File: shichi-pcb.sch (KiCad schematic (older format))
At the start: 27 parts, among them J1 USB_C_Receptacle_HRO_TYPE-C-3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, J2 Conn_01x04_Male, J3 Conn_01x06_Male, J4 Conn_01x04_Male, J5 Conn_01x02_Male, J6 Conn_01x01_Male, SW1 SW_Push, SW2 SW_Push, U1 MCP1700-3302E_SOT23, U2 USBLC6-2SC6, U3 STM32F072CBTx

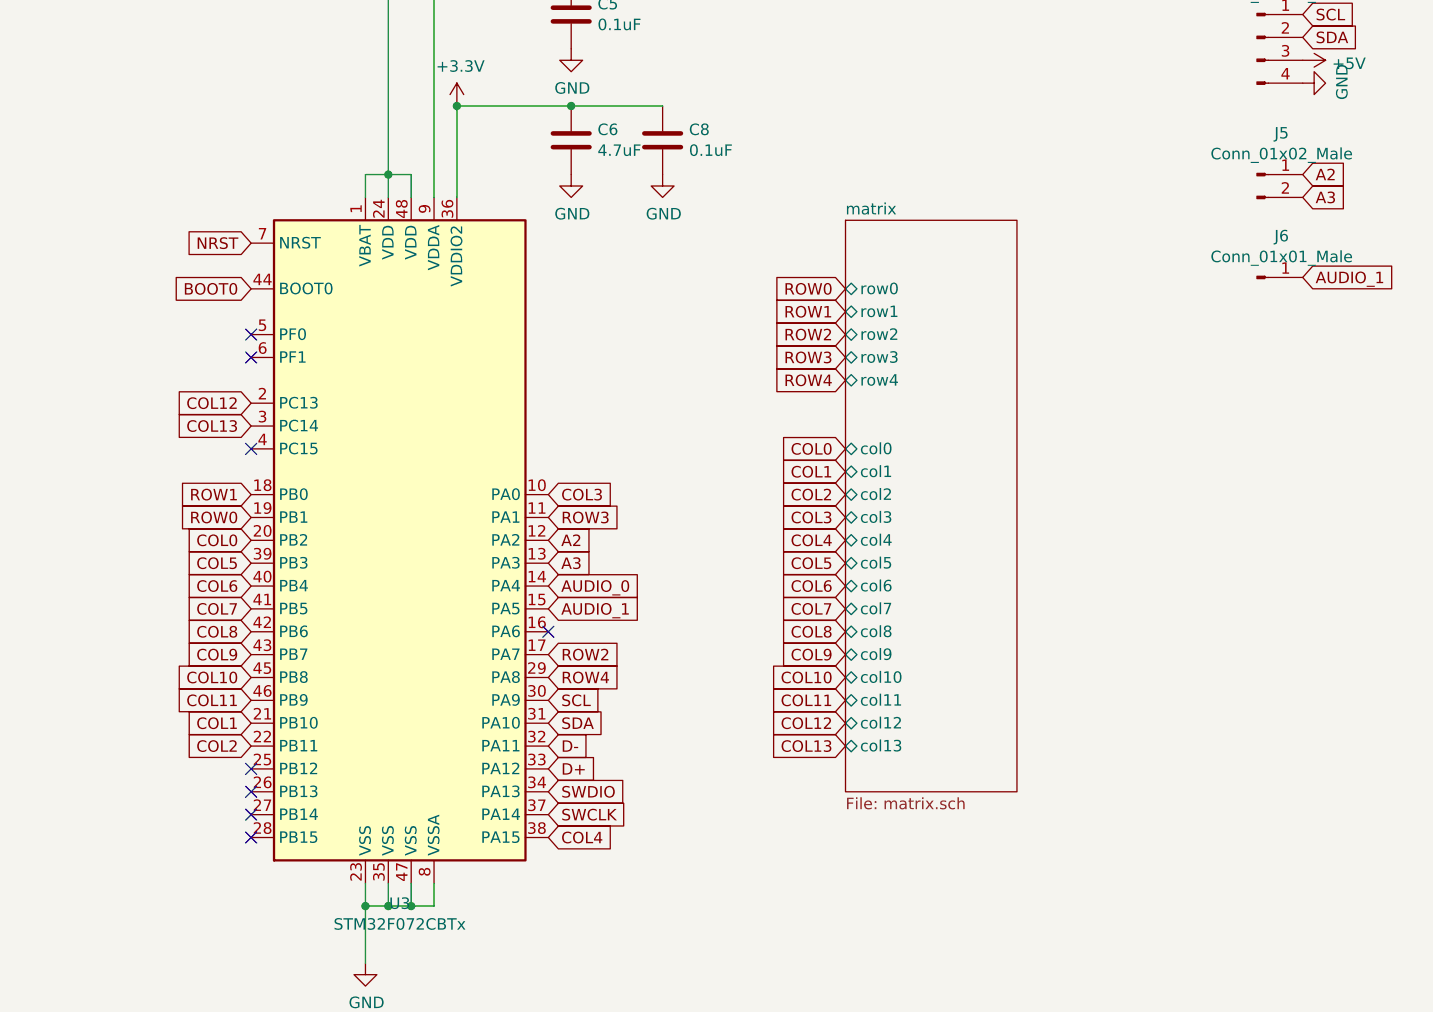
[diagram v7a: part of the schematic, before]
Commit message: Optimize STM32F072 matrix pinout
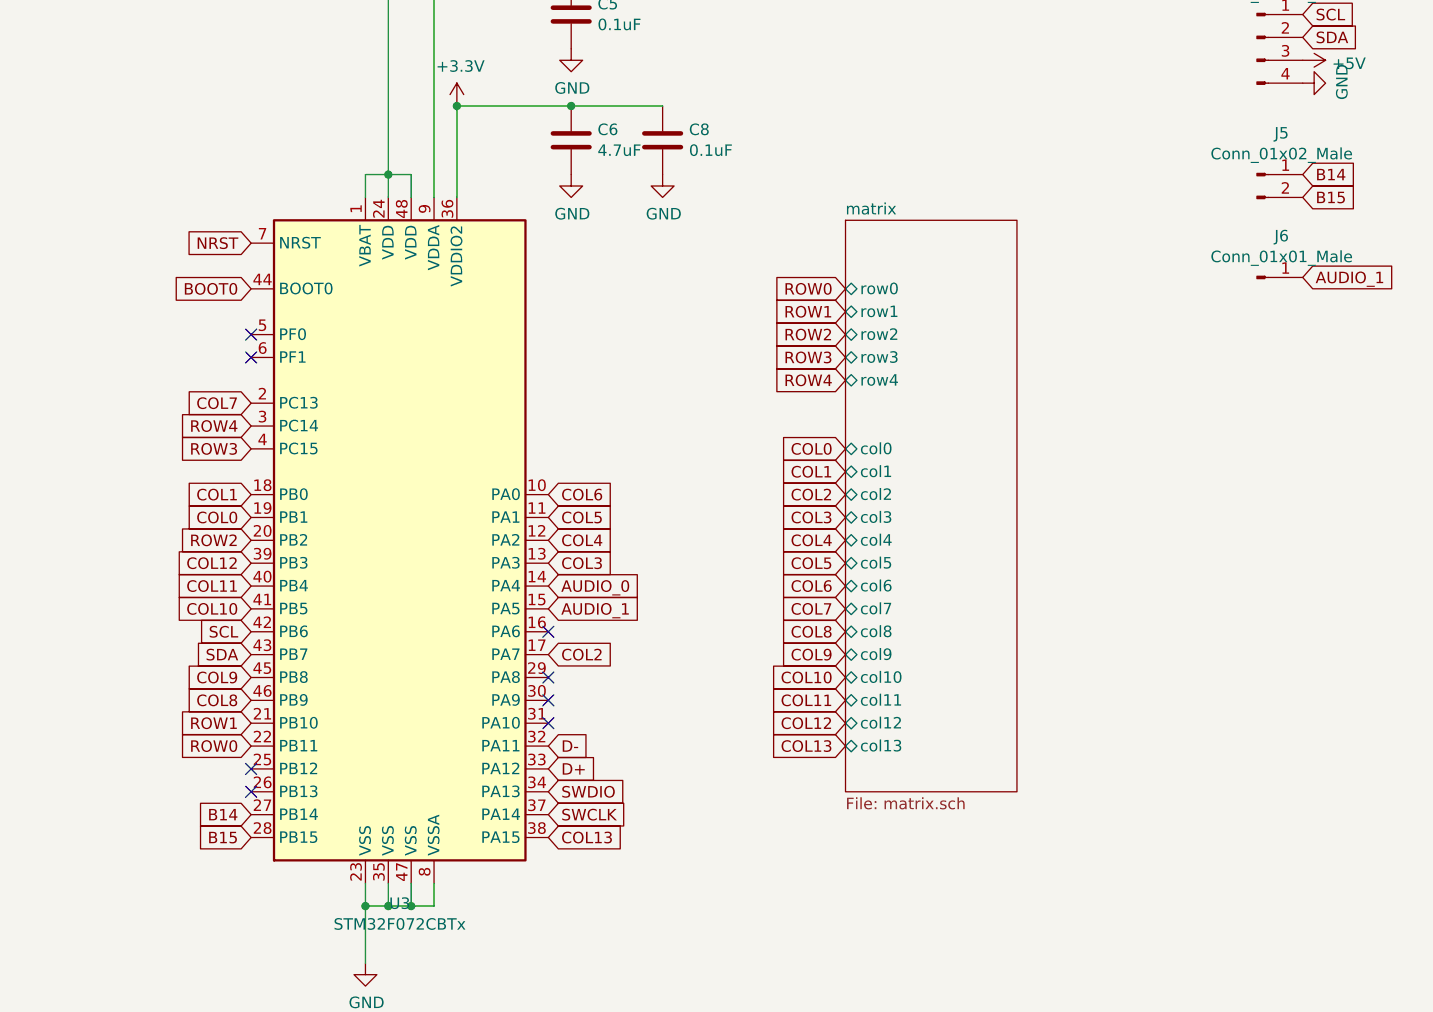
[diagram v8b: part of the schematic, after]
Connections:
- net COL0: now also U3.19 (PB1); no longer U3.20 (PB2)
- net COL1: now also U3.18 (PB0); no longer U3.21 (PB10)
- net COL10: now also U3.41 (PB5); no longer U3.45 (PB8)
- net COL11: now also U3.40 (PB4); no longer U3.46 (PB9)
- net COL12: now also U3.39 (PB3); no longer U3.2 (PC13)
- net COL13: now also U3.38 (PA15); no longer U3.3 (PC14)
- net COL2: now also U3.17 (PA7); no longer U3.22 (PB11)
- net COL3: now also U3.13 (PA3); no longer U3.10 (PA0)
- net COL4: now also U3.12 (PA2); no longer U3.38 (PA15)
- net COL5: now also U3.11 (PA1); no longer U3.39 (PB3)
- net COL6: now also U3.10 (PA0); no longer U3.40 (PB4)
- net COL7: now also U3.2 (PC13); no longer U3.41 (PB5)
- net COL8: now also U3.46 (PB9); no longer U3.42 (PB6)
- net COL9: now also U3.45 (PB8); no longer U3.43 (PB7)
- net ROW0: now also U3.22 (PB11); no longer U3.19 (PB1)
- net ROW1: now also U3.21 (PB10); no longer U3.18 (PB0)
- net ROW2: now also U3.20 (PB2); no longer U3.17 (PA7)
- net ROW3: now also U3.4 (PC15); no longer U3.11 (PA1)
- net ROW4: now also U3.3 (PC14); no longer U3.29 (PA8)
- net SCL: now also U3.42 (PB6); no longer U3.30 (PA9)
- net SDA: now also U3.43 (PB7); no longer U3.31 (PA10)
- net B14: now reaches U3.27 (PB14)
- net B14: now also J5.1 (Pin_1)
- net B15: now reaches U3.28 (PB15)
- net B15: now also J5.2 (Pin_2)
- removed net A2: J5.1 (Pin_1), U3.12 (PA2)
- removed net A3: J5.2 (Pin_2), U3.13 (PA3)
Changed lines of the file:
@@
 Text GLabel 8500 5300 0    50   Input ~ 0
 COL13
+Text GLabel 5900 5300 0    50   Input ~ 0
+ROW0
+Text GLabel 5900 5200 0    50   Input ~ 0
+ROW1
+Text GLabel 5900 4400 0    50   Input ~ 0
+ROW2
+Text GLabel 5900 4000 0    50   Input ~ 0
+ROW3
+Text GLabel 5900 3900 0    50   Input ~ 0
+ROW4
 Text GLabel 5900 4300 0    50   Input ~ 0
-ROW0
+COL0
 Text GLabel 5900 4200 0    50   Input ~ 0
-ROW1
+COL1
 Text GLabel 7200 4900 2    50   Input ~ 0
-ROW2
+COL2
+Text GLabel 7200 4500 2    50   Input ~ 0
+COL3
+Text GLabel 7200 4400 2    50   Input ~ 0
+COL4
 Text GLabel 7200 4300 2    50   Input ~ 0
-ROW3
-Text GLabel 7200 5000 2    50   Input ~ 0
-ROW4
-Text GLabel 5900 4400 0    50   Input ~ 0
-COL0
-Text GLabel 5900 5200 0    50   Input ~ 0
-COL1
-Text GLabel 5900 5300 0    50   Input ~ 0
-COL2
+COL5
 Text GLabel 7200 4200 2    50   Input ~ 0
-COL3
+COL6
+Text GLabel 5900 3800 0    50   Input ~ 0
+COL7
+Text GLabel 5900 5100 0    50   Input ~ 0
+COL8
+Text GLabel 5900 5000 0    50   Input ~ 0
+COL9
+Text GLabel 5900 4700 0    50   Input ~ 0
+COL10
+Text GLabel 5900 4600 0    50   Input ~ 0
+COL11
+Text GLabel 5900 4500 0    50   Input ~ 0
+COL12
 Text GLabel 7200 5700 2    50   Input ~ 0
-COL4
-Text GLabel 5900 4500 0    50   Input ~ 0
-COL5
-Text GLabel 5900 4600 0    50   Input ~ 0
-COL6
-Text GLabel 5900 4700 0    50   Input ~ 0
-COL7
-Text GLabel 5900 4800 0    50   Input ~ 0
-COL8
-Text GLabel 5900 4900 0    50   Input ~ 0
-COL9
-Text GLabel 5900 5000 0    50   Input ~ 0
-COL10
-Text GLabel 5900 5100 0    50   Input ~ 0
-COL11
-Text GLabel 5900 3800 0    50   Input ~ 0
-COL12
-Text GLabel 5900 3900 0    50   Input ~ 0
 COL13
 NoConn ~ 7200 4800
-NoConn ~ 5900 5700
-Text GLabel 7200 5200 2    50   Input ~ 0
+NoConn ~ 7200 5000
+Text GLabel 5900 4900 0    50   Input ~ 0
 SDA
-Text GLabel 7200 5100 2    50   Input ~ 0
+Text GLabel 5900 4800 0    50   Input ~ 0
 SCL
 $Comp
@@
 	1    0    0    -1
 $EndComp
-Text GLabel 7200 4400 2    50   Input ~ 0
-A2
-Text GLabel 7200 4500 2    50   Input ~ 0
-A3
+Text GLabel 5900 5600 0    50   Input ~ 0
+B14
+Text GLabel 5900 5700 0    50   Input ~ 0
+B15
 $Comp
 L power:GND #PWR017
@@
 NoConn ~ 5900 3500
 NoConn ~ 5900 3600
-NoConn ~ 5900 4000
+NoConn ~ 7200 5100
+NoConn ~ 5900 5500
+NoConn ~ 7200 5200
 NoConn ~ 5900 5400
-NoConn ~ 5900 5500
-NoConn ~ 5900 5600
 Text GLabel 10500 2800 2    50   Input ~ 0
-A2
+B14
 Text GLabel 10500 2900 2    50   Input ~ 0
-A3
+B15
 Text GLabel 10500 3250 2    50   Input ~ 0
 AUDIO_1
